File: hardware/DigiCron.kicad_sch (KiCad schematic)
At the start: 11 parts, among them J100 Solder pad, J101 Solder pad, J102 Solder pad, J103 Solder pad, U100 MDBT50Q-U1MV2, U101 HCMS-3917, U102 HCMS-3917, U103 LTR-390UV-01, U104 ADXL345BCCZ-RL, U105 BME280

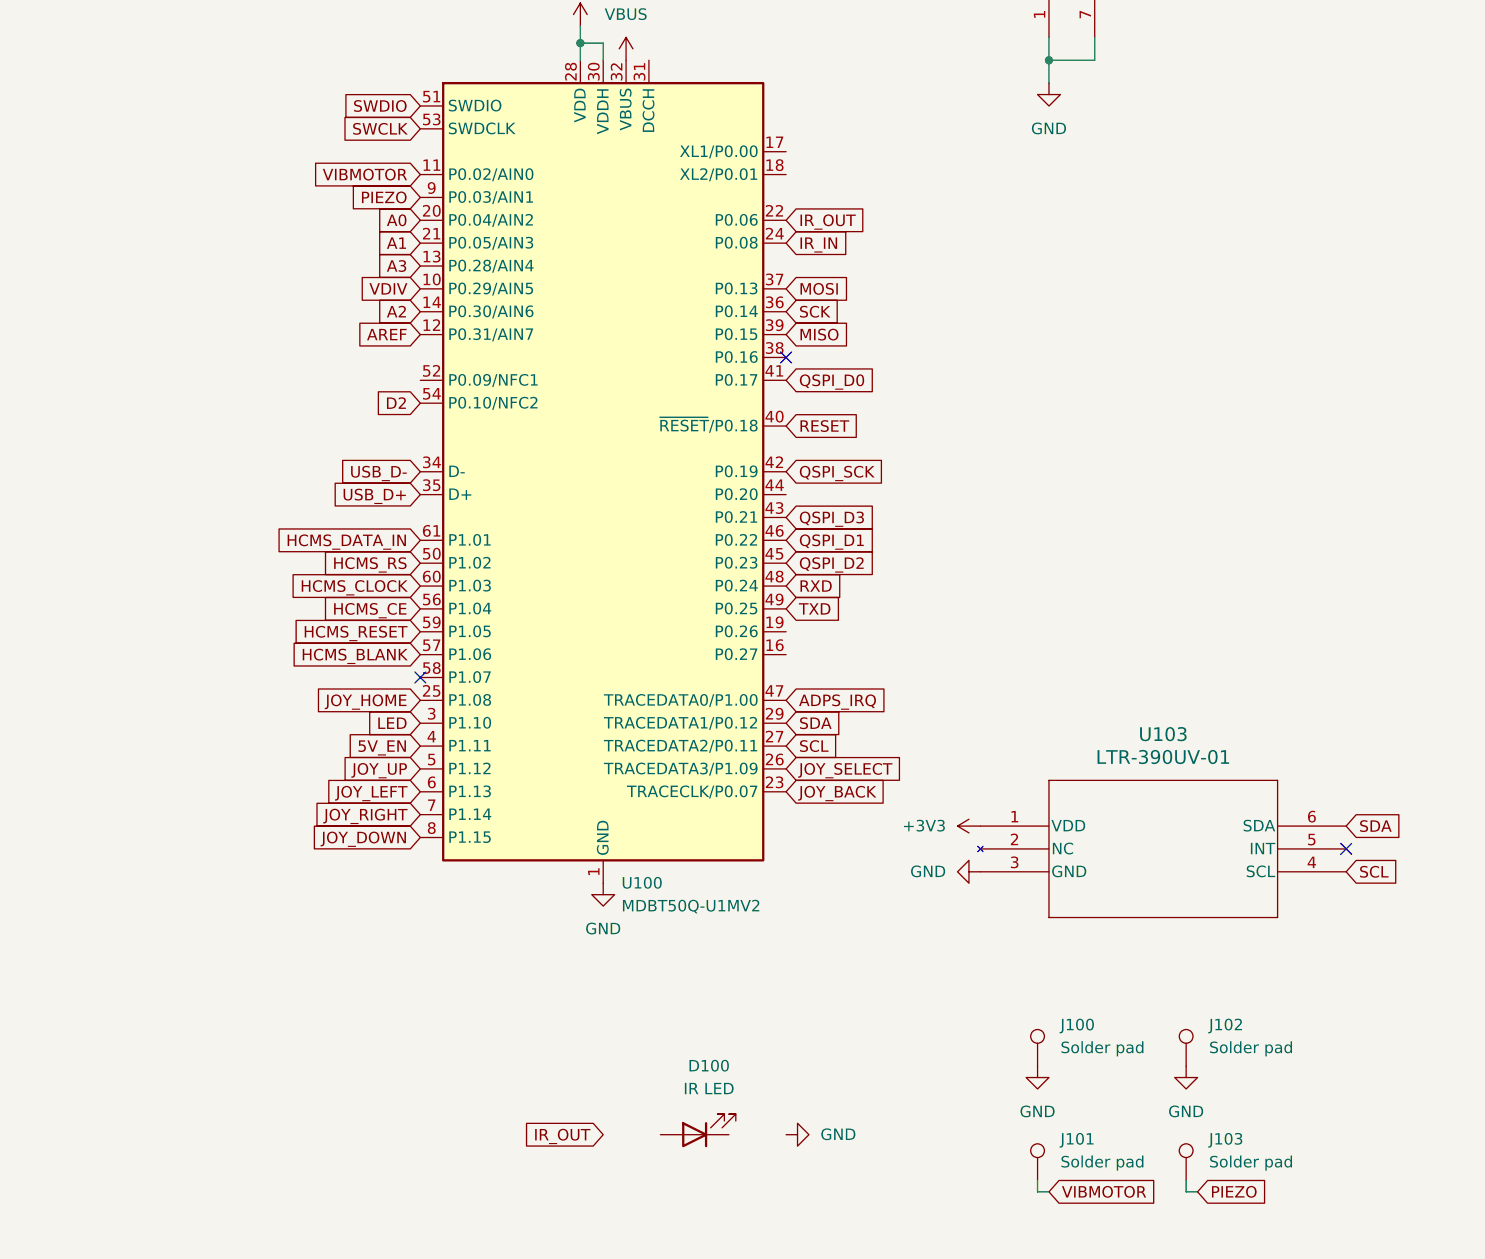
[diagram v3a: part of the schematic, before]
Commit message: Improve power sources for IR LED, vibration motor and piezo buzzer
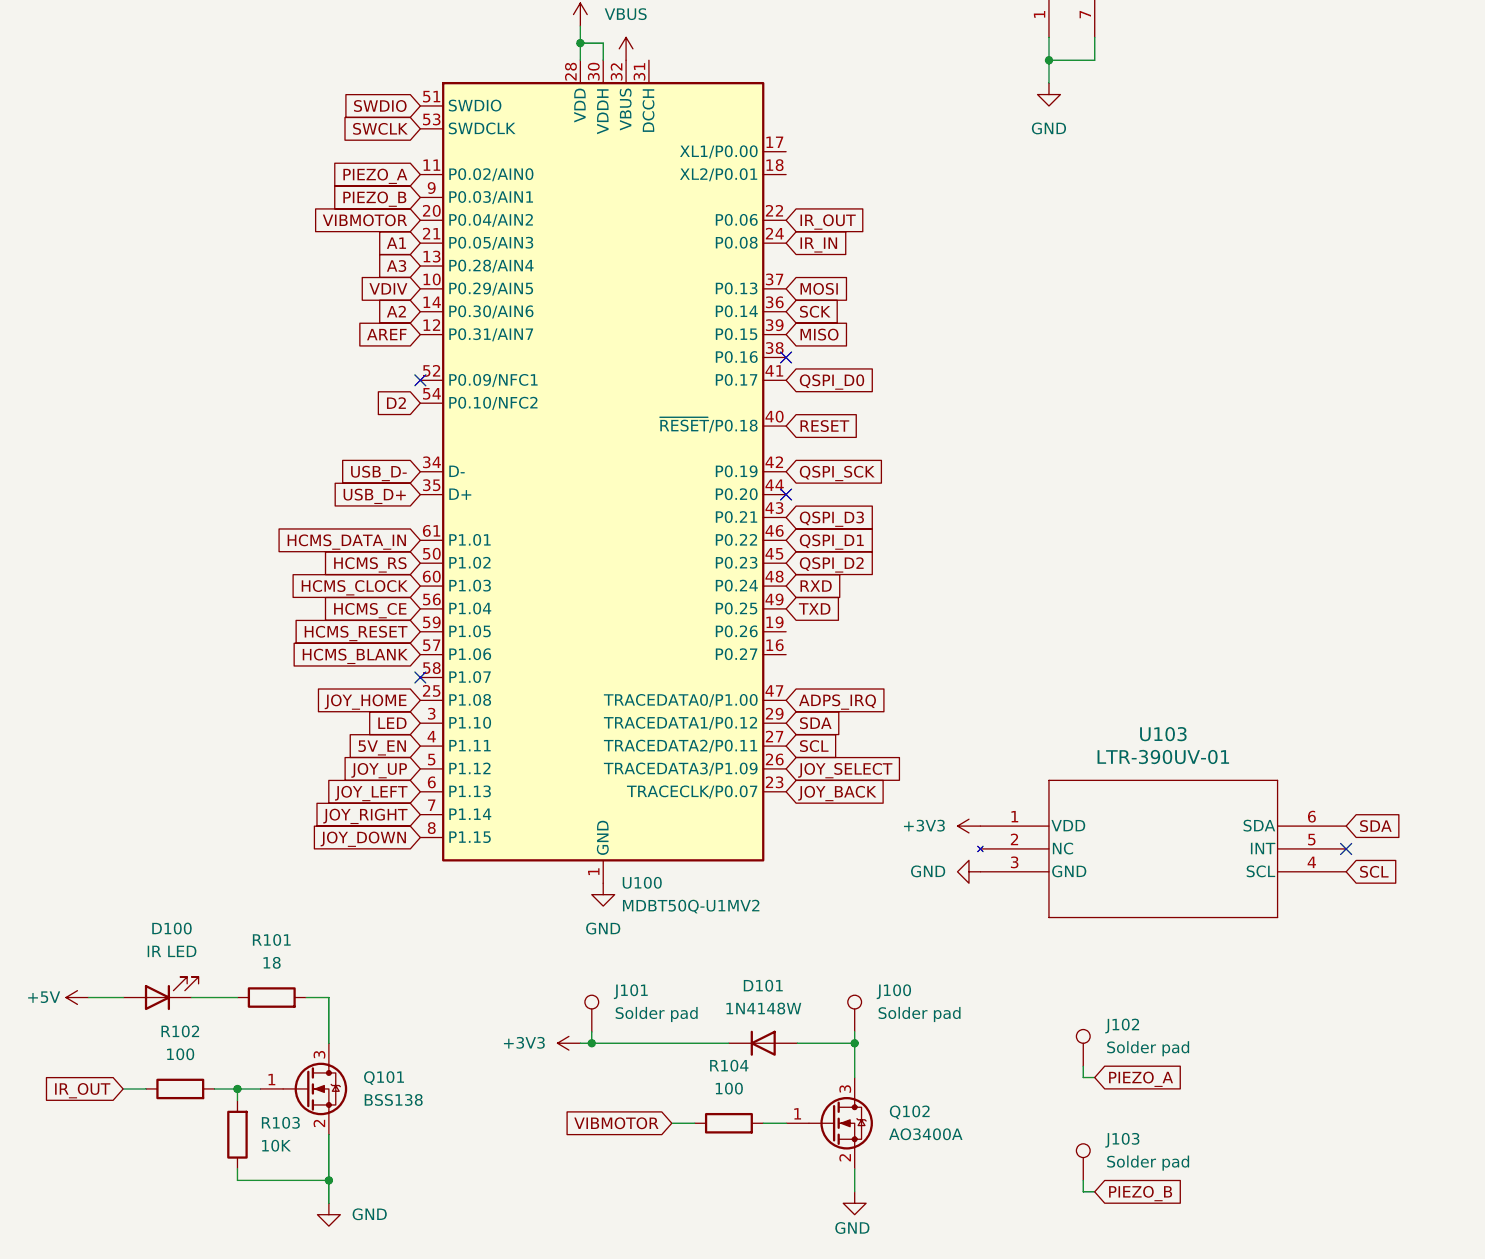
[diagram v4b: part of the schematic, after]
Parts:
- added D101: 1N4148W, Diode_SMD:D_SOD-123, symbol Diode:1N4148W
- added Q101: BSS138, Package_TO_SOT_SMD:SOT-23, symbol Transistor_FET:BSS138
- added Q102: AO3400A, Package_TO_SOT_SMD:SOT-23, symbol Transistor_FET:AO3400A
- added R101: 18, Capacitor_SMD:C_0201_0603Metric_Pad0.64x0.40mm_HandSolder, symbol Device:R
- added R102, R104: 100, Capacitor_SMD:C_0201_0603Metric_Pad0.64x0.40mm_HandSolder, symbol Device:R
- added R103: 10K, Capacitor_SMD:C_0201_0603Metric_Pad0.64x0.40mm_HandSolder, symbol Device:R
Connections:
- net A0 is gone; now on net VIBMOTOR: U100.20 (P0.04/AIN2)
- net +3V3: now also J101.1, D101.1 (K)
- net +5V: now also D100.2 (A)
- net GND: now also Q101.2 (S), Q102.2 (S), R103.1; no longer J100.1, J102.1
- net IR_OUT: now also R102.1
- net VIBMOTOR: now also R104.1; no longer J101.1, U100.11 (P0.02/AIN0)
- net at D100.1 (K): now also R101.1
- net PIEZO renamed PIEZO_B
- new net: Q101.1 (G), R102.2, R103.2
- new net: Q102.1 (G), R104.2
- new net: D101.2 (A), J100.1, Q102.3 (D)
- new net: Q101.3 (D), R101.2
- new net PIEZO_A: J102.1, U100.11 (P0.02/AIN0)
- no-connect marks 13 -> 15
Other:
- moved on the sheet: D100, J100, J101, J102, J103

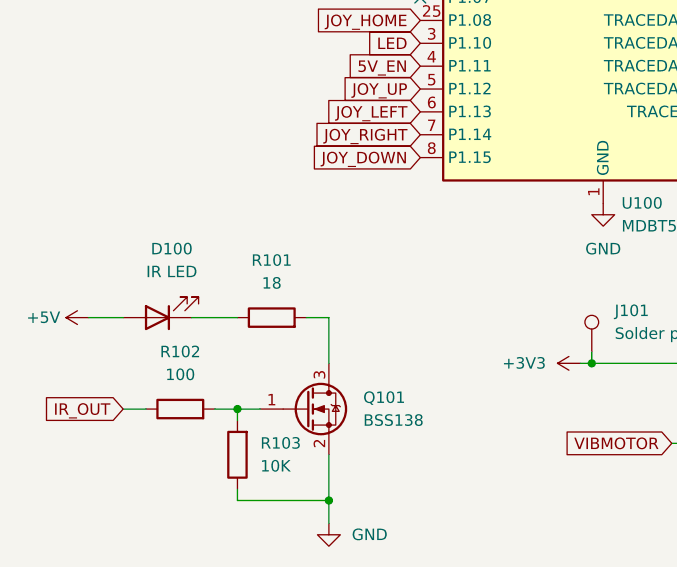
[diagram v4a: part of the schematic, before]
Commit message: Reduce power consumption of IR LED
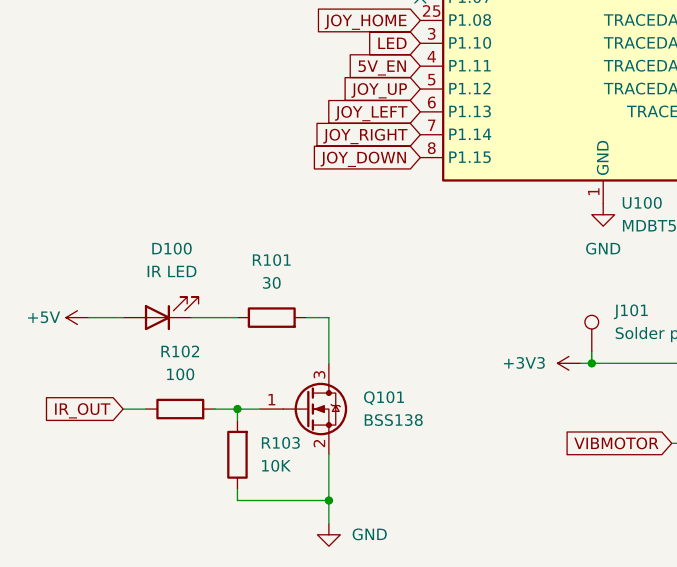
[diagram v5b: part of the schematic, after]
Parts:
- R101: value 18 -> 30
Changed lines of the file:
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@@
 			)
 		)
-		(property "Value" "18"
+		(property "Value" "30"
 			(at 44.45 161.29 90)
 			(effects

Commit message: Add voltage divider and replace boost converter
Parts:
- renumbered Q101 to Q100, Q102 to Q101, R101 to R100, R102 to R101, R103 to R102, R104 to R103
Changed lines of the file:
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@@
 		(dnp no)
 		(fields_autoplaced yes)
-		(property "Reference" "R102"
+		(property "Reference" "R101"
 			(at 34.29 168.91 90)
 			(effects
@@
 			(project "DigiCron"
 				(path "/da54d175-8762-4f8c-be46-30694592bf7b"
-					(reference "R102")
+					(reference "R101")
 					(unit 1)
 				)
@@
 		(dnp no)
 		(fields_autoplaced yes)
-		(property "Reference" "Q102"
+		(property "Reference" "Q101"
 			(at 113.03 177.7999 0)
 			(effects
@@
 			(project ""
 				(path "/da54d175-8762-4f8c-be46-30694592bf7b"
-					(reference "Q102")
+					(reference "Q101")
 					(unit 1)
 				)
@@
 		(dnp no)
 		(fields_autoplaced yes)
-		(property "Reference" "R103"
+		(property "Reference" "R102"
 			(at 43.18 179.0699 0)
 			(effects
@@
 			(project "DigiCron"
 				(path "/da54d175-8762-4f8c-be46-30694592bf7b"
-					(reference "R103")
+					(reference "R102")
 					(unit 1)
 				)
@@
 		(dnp no)
 		(fields_autoplaced yes)
-		(property "Reference" "R104"
+		(property "Reference" "R103"
 			(at 95.25 172.72 90)
 			(effects
@@
 			(project "DigiCron"
 				(path "/da54d175-8762-4f8c-be46-30694592bf7b"
-					(reference "R104")
+					(reference "R103")
 					(unit 1)
 				)
@@
 		(dnp no)
 		(fields_autoplaced yes)
-		(property "Reference" "R101"
+		(property "Reference" "R100"
 			(at 44.45 158.75 90)
 			(effects
@@
 			(project ""
 				(path "/da54d175-8762-4f8c-be46-30694592bf7b"
-					(reference "R101")
+					(reference "R100")
 					(unit 1)
 				)
@@
 		(dnp no)
 		(fields_autoplaced yes)
-		(property "Reference" "Q101"
+		(property "Reference" "Q100"
 			(at 54.61 173.9899 0)
 			(effects
@@
 			(project ""
 				(path "/da54d175-8762-4f8c-be46-30694592bf7b"
-					(reference "Q101")
-					(unit 1)
-				)
+					(reference "Q100")
+					(unit 1)
+				)

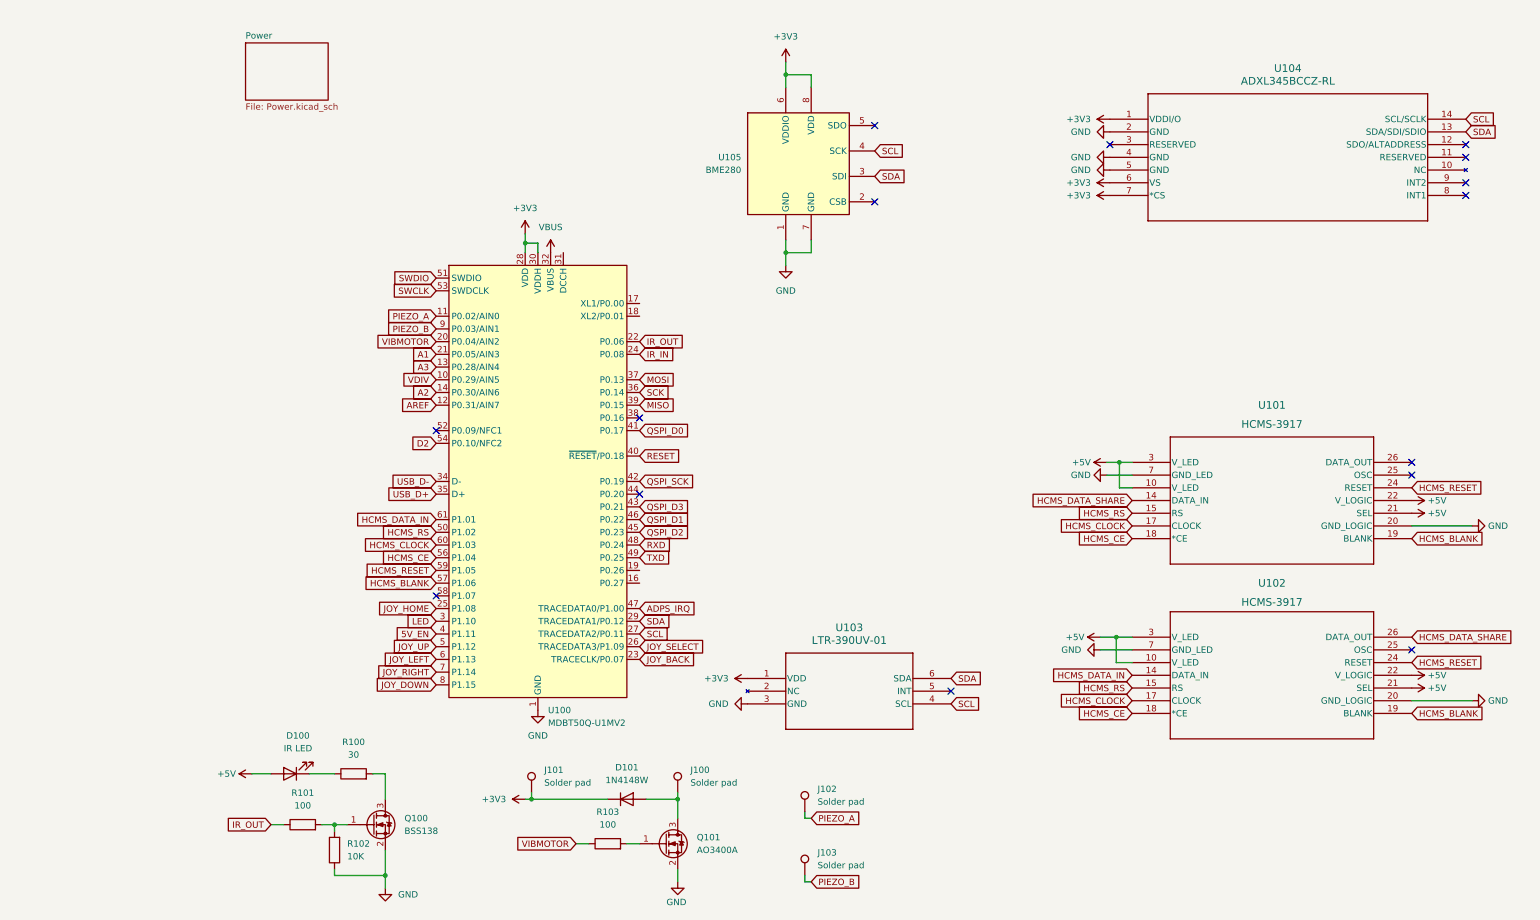
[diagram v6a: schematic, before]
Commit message: Make a few minor adjustments and add headings to schematic
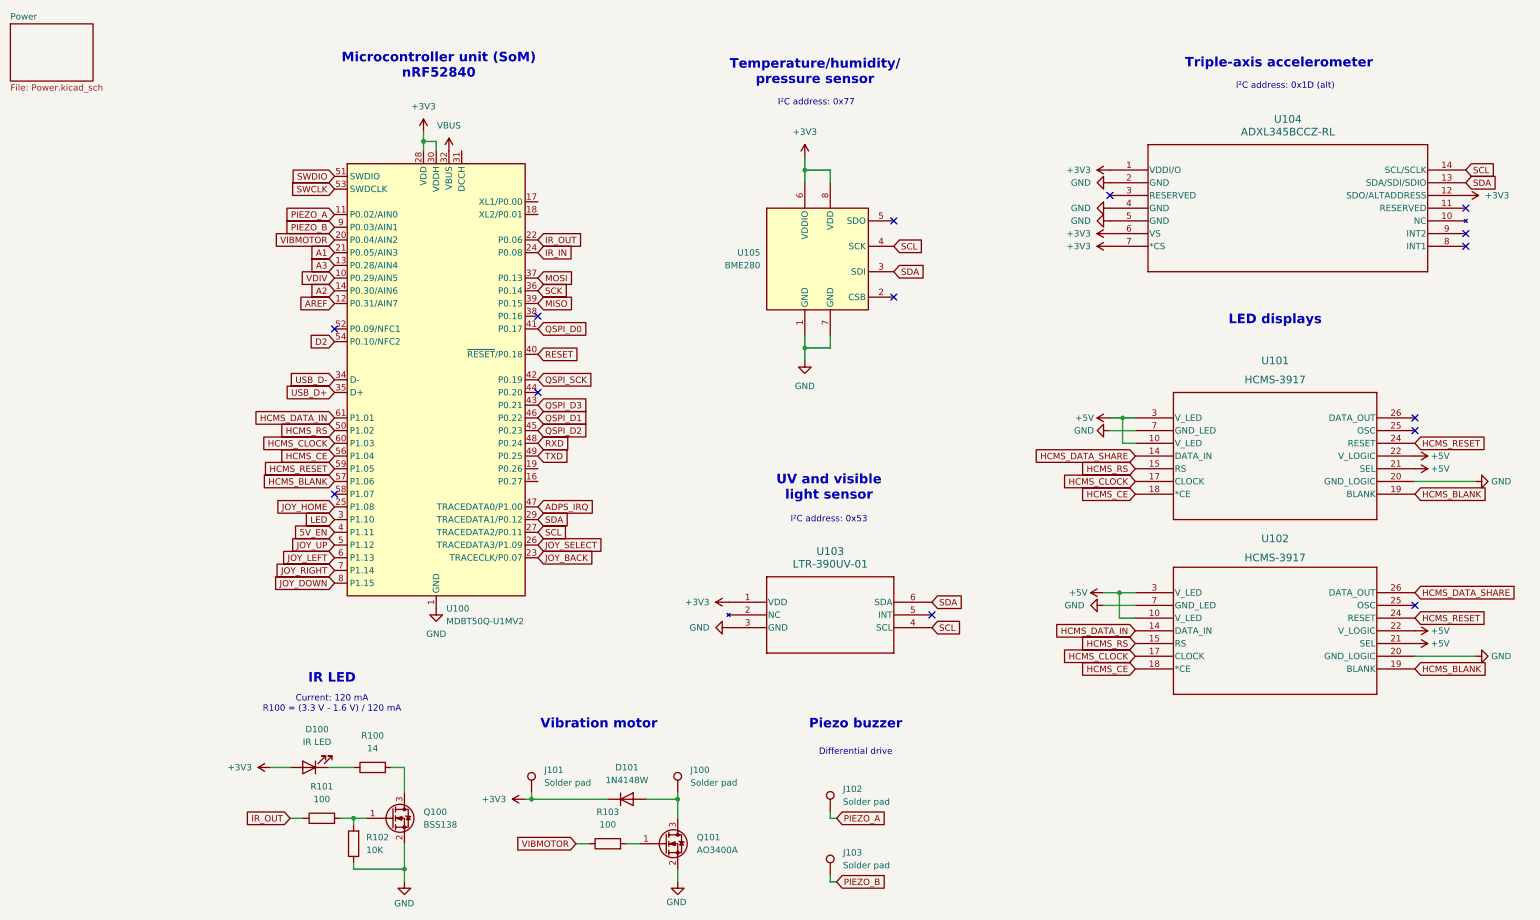
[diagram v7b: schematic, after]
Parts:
- R100: value 30 -> 14
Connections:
- net +3V3: now also D100.2 (A), U104.12 (SDO/ALTADDRESS)
- net +5V: no longer D100.2 (A)
- no-connect marks 15 -> 14
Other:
- note added: "Current: 120 mA R100 = (3.3 V - 1.6 V) / 120 mA"
- note added: "Differential drive"
- note added: "IR LED"
- note added: "I²C address: 0x1D (alt)"
- note added: "I²C address: 0x53"
- note added: "I²C address: 0x77"
- note added: "LED displays"
- note added: "Microcontroller unit (SoM) nRF52840"
- note added: "Piezo buzzer"
- note added: "Temperature/humidity/ pressure sensor"
- note added: "Triple-axis accelerometer"
- note added: "UV and visible light sensor"
- note added: "Vibration motor"
- moved on the sheet: D100, J102, J103, Q100, R100, R101, R102, U100, U101, U102, U103, U104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

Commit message: Add buttons to PCB layout
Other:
- sheet Power renamed Power and input
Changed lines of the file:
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@@
 			(color 0 0 0 0.0000)
 		)
-		(property "Sheetname" "Power"
+		(property "Sheetname" "Power and input"
 			(at -24.13 14.5284 0)
 			(effects
